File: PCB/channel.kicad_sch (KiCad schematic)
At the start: 66 parts, among them J8 Screw_Terminal_01x02, J9 Conn_Coaxial, U13 CC3-0512DF-E, U14 ISO7760, U15 ISO7741, U16 L78L05_SO8, U17 AD5752, U18 AD7321, U19 AD1582, U20 OPA197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

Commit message: Stimjim Rev. B candidate
- Sent to fab
- Lots of manufacturability changes
- BOM consolidation
- Repo layout changed a bit to remove redundant information. e.g.
  datasheet links are embedded in schematic. BOM information embedded in
  schematic. etc
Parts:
- C28, C29, C30, C33, C36, C37, C40, C52: Voltage (none) -> 25V
- C54: now not fitted
- J8: value Screw_Terminal_01x02 -> 1-2834016-2; MPN (none) -> 1-2834016-2; now left out of the parts list
- J9: value Conn_Coaxial -> 0731375003; MPN (none) -> 0731375003
- R10, R11, R12, R13, R14, R18, R8, R9: Tolerance (none) -> 1%
- R20: value 1M -> 2.2M
- U13: MPN (none) -> CC3-0512DF-E
- U14: MPN (none) -> ISO7760DWR
- U15: MPN (none) -> ISO7741DWR
- U16: value L78L05_SO8 -> MC78L05ACDR2G; MPN (none) -> MC78L05ACDR2G
- U17: MPN (none) -> AD5752AREZ
- U18: MPN (none) -> AD7321BRUZ-REEL7
- U19: MPN (none) -> AD1582ARTZ-REEL
- U20: MPN (none) -> OPA197IDR
- U21: MPN (none) -> AMP03GSZ-RL
- U22: MPN (none) -> INA826AIDR
- U23: value DG509ACWE -> DG409DYZ-T; MPN (none) -> DG409DYZ-T

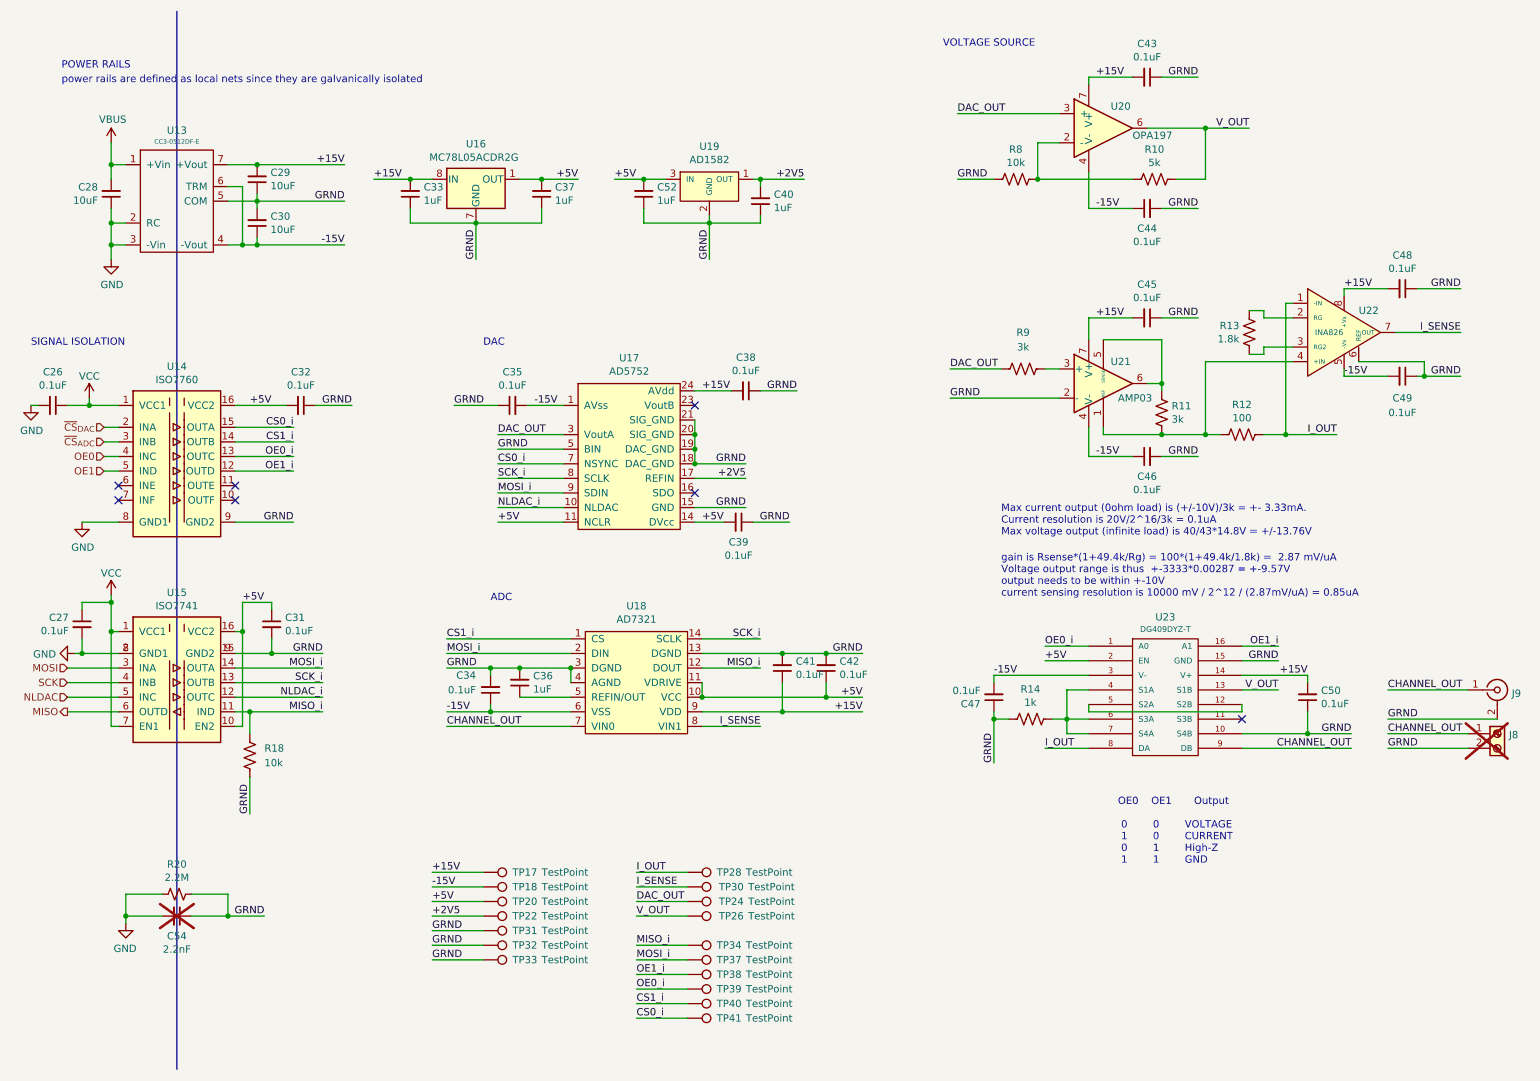
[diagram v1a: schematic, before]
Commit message: Rev C First Draft
- Fix and move LED footprints
- Move bar code sticker
- Add op-amp unity voltage follower to ADC input
- Remove screw terminals
- Made panel screw holes bigger both panels (3.2mm -> 3.7mm) for 3.4mm
  screws
- Create cutout for mounting rail on panels
- Delete the file with both back and front panels
- Update all footprints (except rp2354b so that its thermal vias pass DRC)
- Add component class and custom rule for USB-C footprint
- Indicate M3 screw in schematic + Add to BOM
- Improve adherence to ADC/DAC datasheets:
  - Move high speed signals out from under ADC (put MISO in +5V layer under ADC)
  - Add 10uF decoupling caps to ADC/DAC
- Change enclosure part number to black enclosure
- Add some more GND vias to isolated GND planes
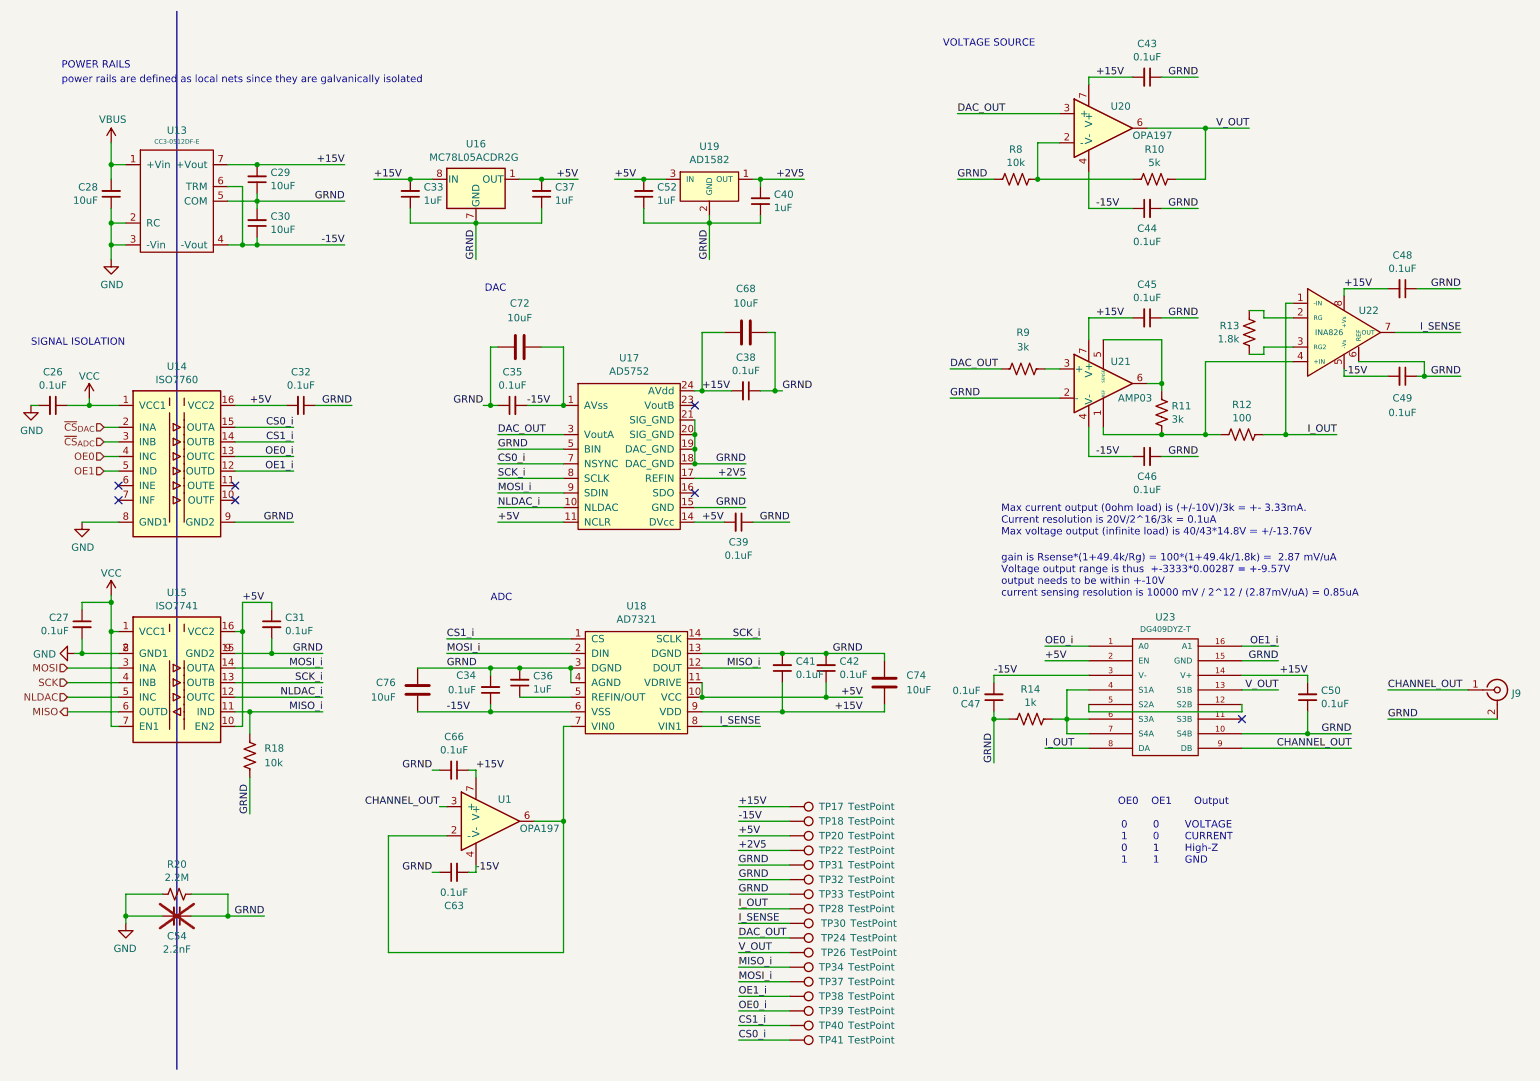
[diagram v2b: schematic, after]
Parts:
- removed J8: 1-2834016-2, microstim:1-2834016-2 _TERM_BLK_2P_SIDE_ENT_2.54MM_PCB, symbol Connector:Screw_Terminal_01x02
- added C63, C66: 0.1uF, Capacitor_SMD:C_0603_1608Metric, symbol Device:C_Small
- added C68, C72, C74, C76: 10uF, Capacitor_SMD:C_0603_1608Metric, symbol Device:C
- added U1: OPA197, Package_SO:SOIC-8_3.9x4.9mm_P1.27mm, symbol stimjimlib:OPA197
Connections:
- net +15V: now also C66.1, C68.1, C74.1, U1.7 (V+)
- net -15V: now also C63.2, C72.2, C76.2, U1.4 (V-)
- net CHANNEL_OUT: now also U1.3 (+); no longer U18.7 (VIN0)
- net GRND: now also C63.1, C66.2, C68.2, C72.1, C74.2, C76.1
- new net: U1.2 (-), U1.6, U18.7 (VIN0)
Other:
- moved on the sheet: TP17, TP18, TP20, TP22, TP24, TP26, TP28, TP30, TP31, TP32, TP33, TP34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

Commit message: Replace amplifiers
- INA826 -> AD8421
- AMP03 -> LT1995 w/ op-amp in feedback circuit
- Also:
  - update to kicad v10
  - utilize multi-channel layout feature
  - update calculations on schematic
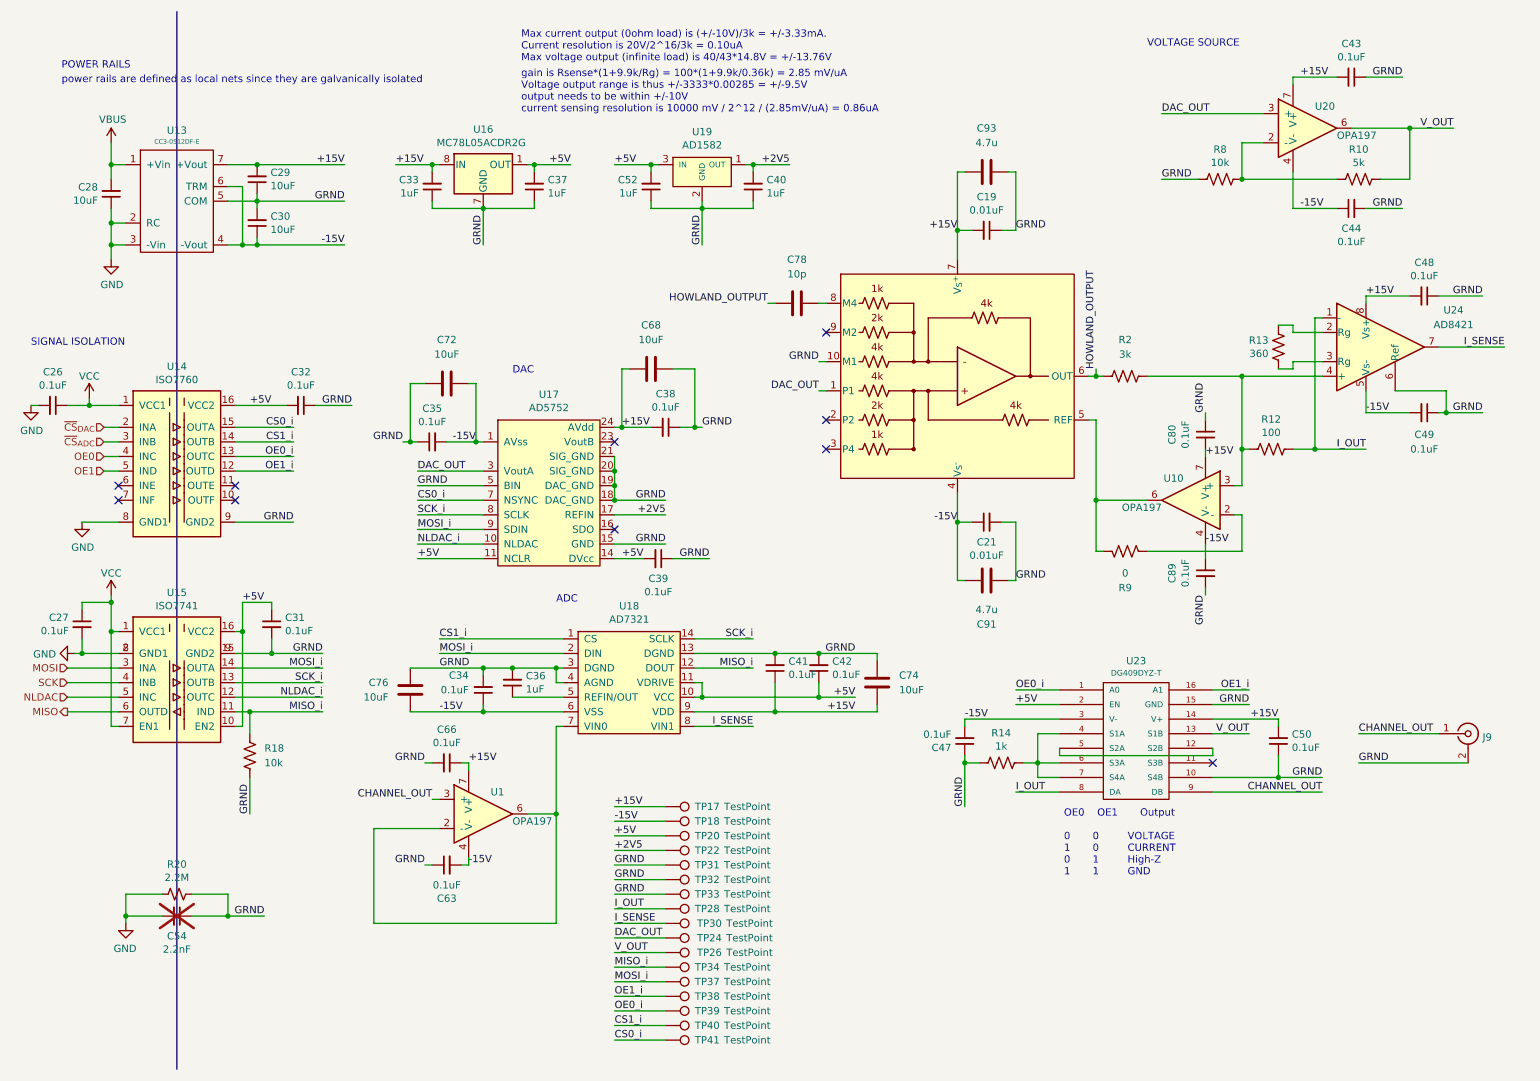
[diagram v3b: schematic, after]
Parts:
- removed C45, C46: 0.1uF, Capacitor_SMD:C_0603_1608Metric, symbol Device:C_Small
- removed R11: 3k, Resistor_SMD:R_0603_1608Metric, symbol Device:R_US
- removed U21: AMP03, Package_SO:SOIC-8_3.9x4.9mm_P1.27mm, symbol stimjimlib:AMP03
- removed U22: INA826, Package_SO:SOIC-8_3.9x4.9mm_P1.27mm, symbol stimjimlib:INA826
- added C19, C21: 0.01uF, Capacitor_SMD:C_0603_1608Metric, symbol Device:C_Small
- added C78: 10p, Capacitor_SMD:C_0603_1608Metric, symbol Device:C
- added C80, C89: 0.1uF, Capacitor_SMD:C_0603_1608Metric, symbol Device:C_Small
- added C91, C93: 4.7u, Capacitor_SMD:C_0603_1608Metric, symbol Device:C
- added R2: 3k, Resistor_SMD:R_0603_1608Metric, symbol Device:R_US
- added U10: OPA197, Package_SO:SOIC-8_3.9x4.9mm_P1.27mm, symbol stimjimlib:OPA197
- added U24: AD8421, Package_SO:SOIC-8_3.9x4.9mm_P1.27mm, symbol Amplifier_Instrumentation:AD8421BRZ
- added U27: LT1995, Package_SO:MSOP-10_3x3mm_P0.5mm, symbol open-ephys:LT1995
- R13: value 1.8k -> 360
- R9: value 3k -> 0; Tolerance 1% -> (none)
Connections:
- net +15V: now also C19.2, C80.2, C93.2, U10.7 (V+), U24.8 (Vs+), U27.7 (V_{S}^{+})
- net -15V: now also C21.1, C89.1, C91.2, U10.4 (V-), U24.5 (Vs-), U27.4 (V_{S}^{-})
- net DAC_OUT: now also U27.1 (P1); no longer R9.2
- net GRND: now also C19.1, C21.2, C80.1, C89.2, C91.1, C93.1, U24.6 (Ref), U27.10 (M1)
- net I_OUT: now also U24.1 (-)
- net I_SENSE: now also U24.7
- net at R12.1: now also R2.2, U10.3 (+), U24.4 (+)
- net at R13.1: now also U24.3 (Rg)
- net at R13.2: now also U24.2 (Rg)
- net at R9.1: now also U10.6, U27.5 (REF)
- new net: R9.2, U10.2 (-)
- new net: C78.2, U27.8 (M4)
- new net HOWLAND_OUTPUT: C78.1, R2.1, U27.6 (OUT)
- no-connect marks 7 -> 10
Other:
- note added: "Max current output (0ohm load) is (+/-10V)/3k = +/-3.33mA. Current resolution is 20V/2^16/3k = 0.10uA Max voltage output (infinite load) is 40/43*14.8V = +/-13.76V"
- note added: "gain is Rsense*(1+9.9k/Rg) = 100*(1+9.9k/0.36k) = 2.85 mV/uA Voltage output range is thus +/-3333*0.00285 = +/-9.5V output needs to be within +/-10V current sensing resolution is 10000 mV / 2^12 / (2.85mV/uA) = 0.86uA"
- note removed: "Max current output (0ohm load) is (+/-10V)/3k = +- 3.33mA. Current resolution is 20V/2^16/3k = 0.1uA Max voltage output (infinite load) is 40/43*14.8V = +/-13.76V"
- note removed: "gain is Rsense*(1+49.4k/Rg) = 100*(1+49.4k/1.8k) = 2.87 mV/uA Voltage output range is thus +-3333*0.00287 = +-9.57V output needs to be within +-10V current sensing resolution is 10000 mV / 2^12 / (2.87mV/uA) = 0.85uA"
- moved on the sheet: C33, C34, C35, C36, C37, C38, C39, C40, C41, C42, C43, C44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

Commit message: tolerance resistors
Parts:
- R10, R12, R13, R8: Tolerance 1% -> 0.1%
- R2: Tolerance (none) -> 1%
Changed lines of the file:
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@@
 			)
 		)
+		(property "Tolerance" "1%"
+			(at 213.36 76.2 90)
+			(hide yes)
+			(show_name no)
+			(do_not_autoplace no)
+			(effects
+				(font
+					(size 1.27 1.27)
+				)
+			)
+		)
 		(pin "2"
 		)
@@
 			)
 		)
-		(property "Tolerance" "1%"
+		(property "Tolerance" "0.1%"
 			(at 238.76 88.9 90)
 			(hide yes)
@@
 			)
 		)
-		(property "Tolerance" "1%"
+		(property "Tolerance" "0.1%"
 			(at 229.87 41.91 90)
 			(hide yes)
@@
 			)
 		)
-		(property "Tolerance" "1%"
+		(property "Tolerance" "0.1%"
 			(at 240.03 71.12 0)
 			(hide yes)
@@
 			)
 		)
-		(property "Tolerance" "1%"
+		(property "Tolerance" "0.1%"
 			(at 254 41.91 90)
 			(hide yes)
